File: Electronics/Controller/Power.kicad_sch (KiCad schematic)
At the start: 27 parts, among them J10 TABLET 1 PWR, J11 TABLET 2 PWR, J9 TRACTOR BATTERY, U5 LM2596S-5, U6 LM2587S-ADJ/NOPB, U7 LM2587S-ADJ/NOPB

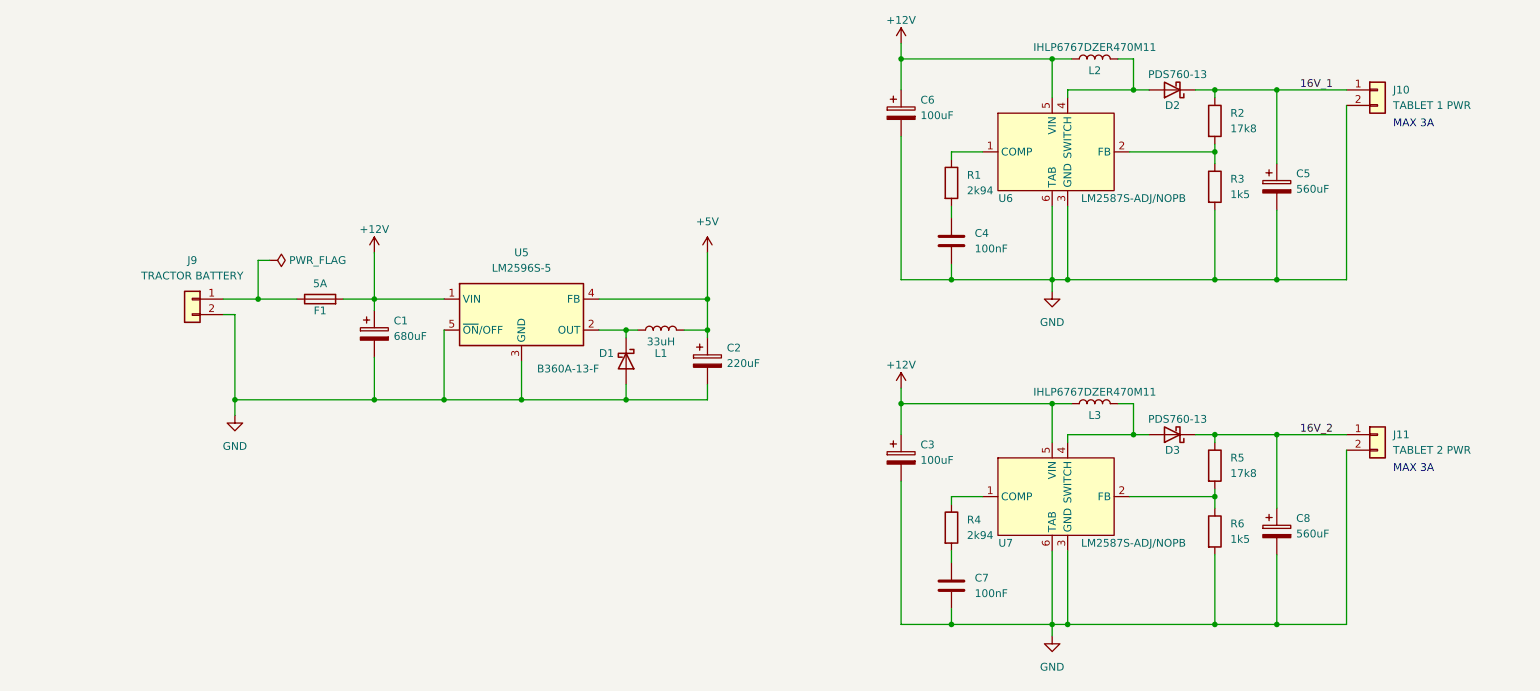
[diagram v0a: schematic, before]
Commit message: Working on schematic. Added datasheets.
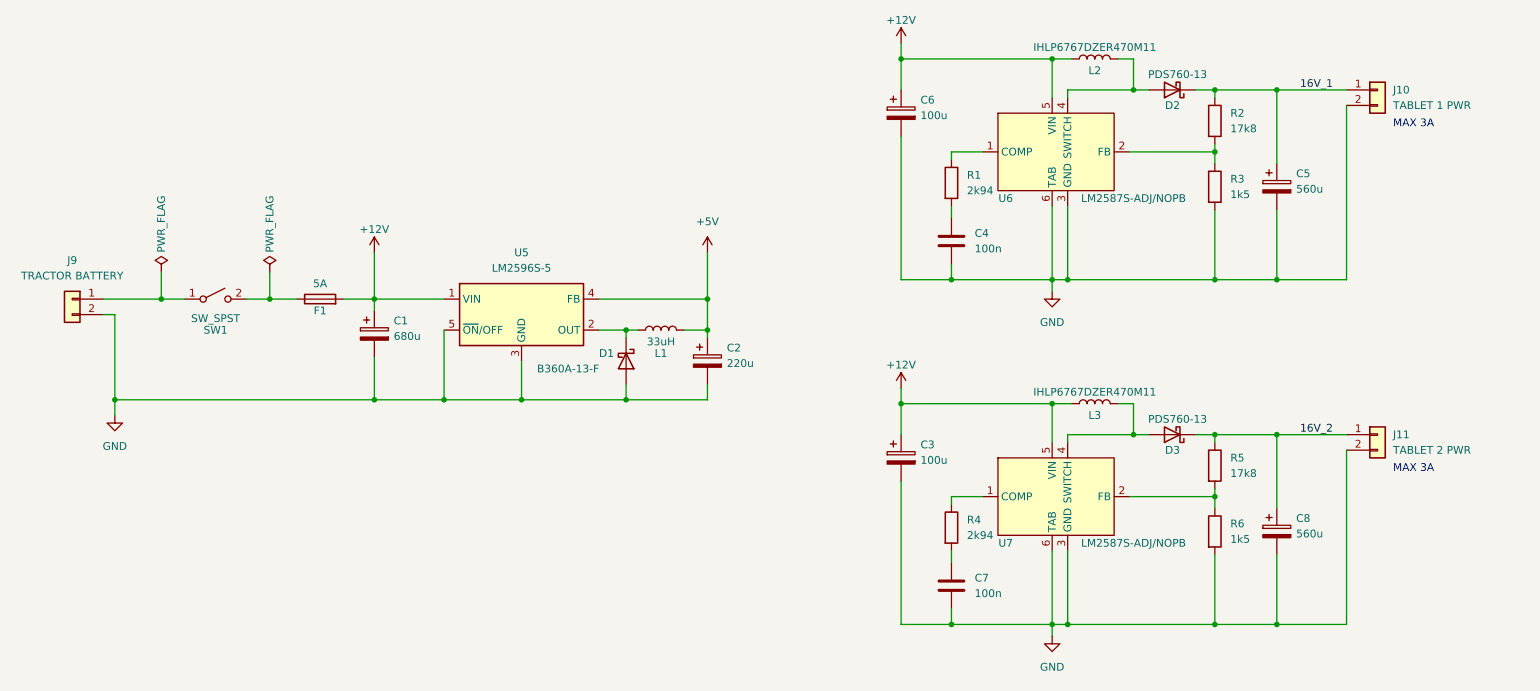
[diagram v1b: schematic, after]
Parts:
- added SW1: SW_SPST, symbol Switch:SW_SPST
- C1: value 680uF -> 680u
- C2: value 220uF -> 220u
- C3, C6: value 100uF -> 100u
- C4, C7: value 100nF -> 100n
- C5, C8: value 560uF -> 560u
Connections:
- net at J9.1 (Pin_1): now also SW1.1 (A); no longer F1.1
- new net: F1.1, SW1.2 (B)
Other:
- moved on the sheet: J9

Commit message: Working on schematic.
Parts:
- added J21: VALVE POWER, symbol Connector:Screw_Terminal_01x04
- F1: value 5A -> 10A
- SW1: value SW_SPST -> ON/OFF
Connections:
- net +12V: now also J21.1 (Pin_1), J21.3 (Pin_3)
- net GND: now also J21.2 (Pin_2), J21.4 (Pin_4)
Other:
- note added: "3A"
- note added: "3A per valve (=6A) 1.5A per tabler (=3A)"
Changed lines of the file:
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@@
   (title_block
     (title "Tandem Leveller Controller")
-    (date "2025-02-14")
+    (date "2025-02-16")
     (rev "V1.0")
     (company "(C) andy@britishideas.com 2025")
@@
   (junction (at 76.835 91.44) (diameter 0) (color 0 0 0 0)
   )
+  (junction (at 93.345 144.145) (diameter 0) (color 0 0 0 0)
+  )
   (junction (at 187.96 88.265) (diameter 0) (color 0 0 0 0)
   )
   (junction (at 171.45 144.78) (diameter 0) (color 0 0 0 0)
   )
+  (junction (at 91.44 136.525) (diameter 0) (color 0 0 0 0)
+  )
   (junction (at 163.195 108.585) (diameter 0) (color 0 0 0 0)
   )
@@
     (stroke (width 0) (type default))
   )
+  (wire (pts (xy 98.425 136.525) (xy 91.44 136.525))
+    (stroke (width 0) (type default))
+  )
   (wire (pts (xy 41.91 86.995) (xy 41.91 91.44))
     (stroke (width 0) (type default))
@@
     (stroke (width 0) (type default))
   )
+  (wire (pts (xy 93.345 139.065) (xy 93.345 144.145))
+    (stroke (width 0) (type default))
+  )
   (wire (pts (xy 131.445 91.44) (xy 131.445 96.52))
     (stroke (width 0) (type default))
@@
     (stroke (width 0) (type default))
   )
+  (wire (pts (xy 93.345 144.145) (xy 93.345 147.32))
+    (stroke (width 0) (type default))
+  )
   (wire (pts (xy 224.79 88.265) (xy 214.63 88.265))
     (stroke (width 0) (type default))
@@
     (stroke (width 0) (type default))
   )
+  (wire (pts (xy 91.44 141.605) (xy 91.44 136.525))
+    (stroke (width 0) (type default))
+  )
   (wire (pts (xy 163.195 106.045) (xy 163.195 108.585))
     (stroke (width 0) (type default))
@@
     (stroke (width 0) (type default))
   )
+  (wire (pts (xy 98.425 144.145) (xy 93.345 144.145))
+    (stroke (width 0) (type default))
+  )
   (wire (pts (xy 236.22 116.205) (xy 236.22 144.78))
     (stroke (width 0) (type default))
@@
     (stroke (width 0) (type default))
   )
+  (wire (pts (xy 98.425 141.605) (xy 91.44 141.605))
+    (stroke (width 0) (type default))
+  )
   (wire (pts (xy 100.965 107.95) (xy 88.265 107.95))
     (stroke (width 0) (type default))
@@
     (stroke (width 0) (type default))
   )
+  (wire (pts (xy 98.425 139.065) (xy 93.345 139.065))
+    (stroke (width 0) (type default))
+  )
   (wire (pts (xy 163.195 121.285) (xy 163.195 144.78))
     (stroke (width 0) (type default))
@@
   )
   (wire (pts (xy 236.22 59.69) (xy 236.22 88.265))
+    (stroke (width 0) (type default))
+  )
+  (wire (pts (xy 91.44 136.525) (xy 91.44 133.35))
     (stroke (width 0) (type default))
   )
@@
     (effects (font (size 1.27 1.27)) (justify left bottom))
   )
+  (text "3A per valve (=6A)\n1.5A per tabler (=3A)" (at 56.515 71.12 0)
+    (effects (font (size 1.27 1.27)) (justify left bottom))
+  )
+  (text "3A" (at 106.68 144.78 0)
+    (effects (font (size 1.27 1.27)) (justify left bottom))
+  )
   (label "16V_1" (at 228.6 57.15 0) (fields_autoplaced)
     (effects (font (size 1.27 1.27)) (justify left bottom))
@@
         (path "/56ffd1a6-bbed-43b6-8aa8-f23f49f76448/dcf28da0-a625-49c3-8f0d-066b6ff7258a"
           (reference "J10") (unit 1)
+        )
+      )
+    )
+  )
+  (symbol (lib_id "power:GND") (at 93.345 147.32 0) (unit 1)
+    (in_bom yes) (on_board yes) (dnp no) (fields_autoplaced)
+    (property "Reference" "#PWR087" (at 93.345 153.67 0)
+      (effects (font (size 1.27 1.27)) hide)
+    )
+    (property "Value" "GND" (at 93.345 152.4 0)
+      (effects (font (size 1.27 1.27)))
+    )
+    (property "Footprint" "" (at 93.345 147.32 0)
+      (effects (font (size 1.27 1.27)) hide)
+    )
+    (property "Datasheet" "" (at 93.345 147.32 0)
+      (effects (font (size 1.27 1.27)) hide)
+    )
+    (pin "1")
+    (instances
+      (project "Tandem Leveller Controller"
+        (path "/56ffd1a6-bbed-43b6-8aa8-f23f49f76448/dcf28da0-a625-49c3-8f0d-066b6ff7258a"
+          (reference "#PWR087") (unit 1)
+        )
+      )
+    )
+  )
+  (symbol (lib_id "power:+12V") (at 91.44 133.35 0) (unit 1)
+    (in_bom yes) (on_board yes) (dnp no)
+    (property "Reference" "#PWR088" (at 91.44 137.16 0)
+      (effects (font (size 1.27 1.27)) hide)
+    )
+    (property "Value" "+12V" (at 91.44 129.54 0)
+      (effects (font (size 1.27 1.27)))
+    )
+    (property "Footprint" "" (at 91.44 133.35 0)
+      (effects (font (size 1.27 1.27)) hide)
+    )
+    (property "Datasheet" "" (at 91.44 133.35 0)
+      (effects (font (size 1.27 1.27)) hide)
+    )
+    (pin "1")
+    (instances
+      (project "Tandem Leveller Controller"
+        (path "/56ffd1a6-bbed-43b6-8aa8-f23f49f76448/dcf28da0-a625-49c3-8f0d-066b6ff7258a"
+          (reference "#PWR088") (unit 1)
         )
       )
@@
     )
   )
+  (symbol (lib_id "Connector:Screw_Terminal_01x04") (at 103.505 139.065 0) (unit 1)
+    (in_bom yes) (on_board yes) (dnp no) (fields_autoplaced)
+    (property "Reference" "J21" (at 106.68 139.065 0)
+      (effects (font (size 1.27 1.27)) (justify left))
+    )
+    (property "Value" "VALVE POWER" (at 106.68 141.605 0)
+      (effects (font (size 1.27 1.27)) (justify left))
+    )
+    (property "Footprint" "" (at 103.505 139.065 0)
+      (effects (font (size 1.27 1.27)) hide)
+    )
+    (property "Datasheet" "~" (at 103.505 139.065 0)
+      (effects (font (size 1.27 1.27)) hide)
+    )
+    (pin "3")
+    (pin "4")
+    (pin "1")
+    (pin "2")
+    (instances
+      (project "Tandem Leveller Controller"
+        (path "/56ffd1a6-bbed-43b6-8aa8-f23f49f76448/dcf28da0-a625-49c3-8f0d-066b6ff7258a"
+          (reference "J21") (unit 1)
+        )
+      )
+    )
+  )
   (symbol (lib_id "Device:C_Polarized") (at 163.195 60.96 0) (unit 1)
     (in_bom yes) (on_board yes) (dnp no)
@@
   (symbol (lib_id "Switch:SW_SPST") (at 50.8 91.44 0) (unit 1)
     (in_bom yes) (on_board yes) (dnp no)
-    (property "Reference" "SW1" (at 50.8 96.52 0)
-      (effects (font (size 1.27 1.27)))
-    )
-    (property "Value" "SW_SPST" (at 50.8 94.615 0)
+    (property "Reference" "SW1" (at 50.8 88.265 0)
+      (effects (font (size 1.27 1.27)))
+    )
+    (property "Value" "ON/OFF" (at 50.8 94.615 0)
       (effects (font (size 1.27 1.27)))
     )
@@
       (effects (font (size 1.27 1.27)))
     )
-    (property "Value" "5A" (at 67.945 88.9 90)
-      (effects (font (size 1.27 1.27)))
-    )
+    (property "Value" "10A" (at 67.945 88.9 90)
+      (effects (font (size 1.27 1.27)))
+    )

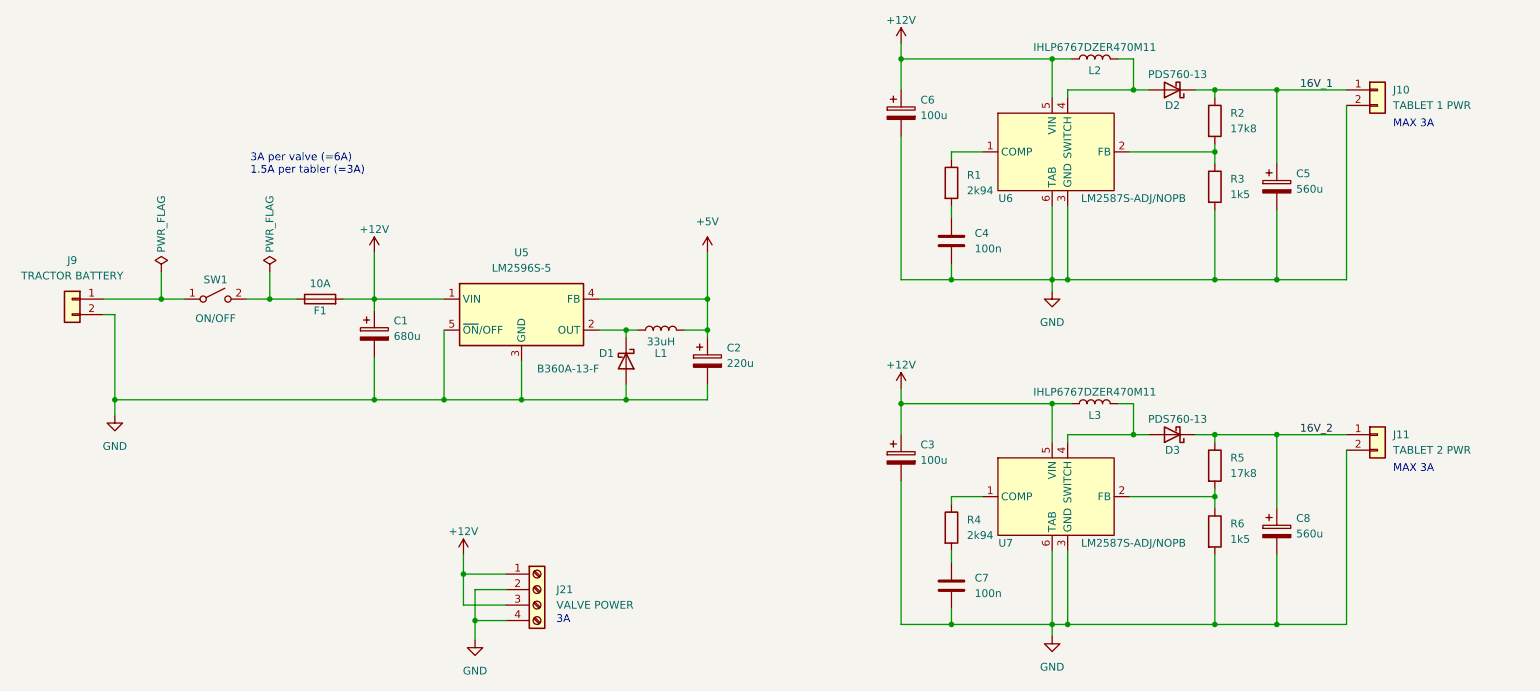
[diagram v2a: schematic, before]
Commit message: Updated schematic. Added footprints for all components.
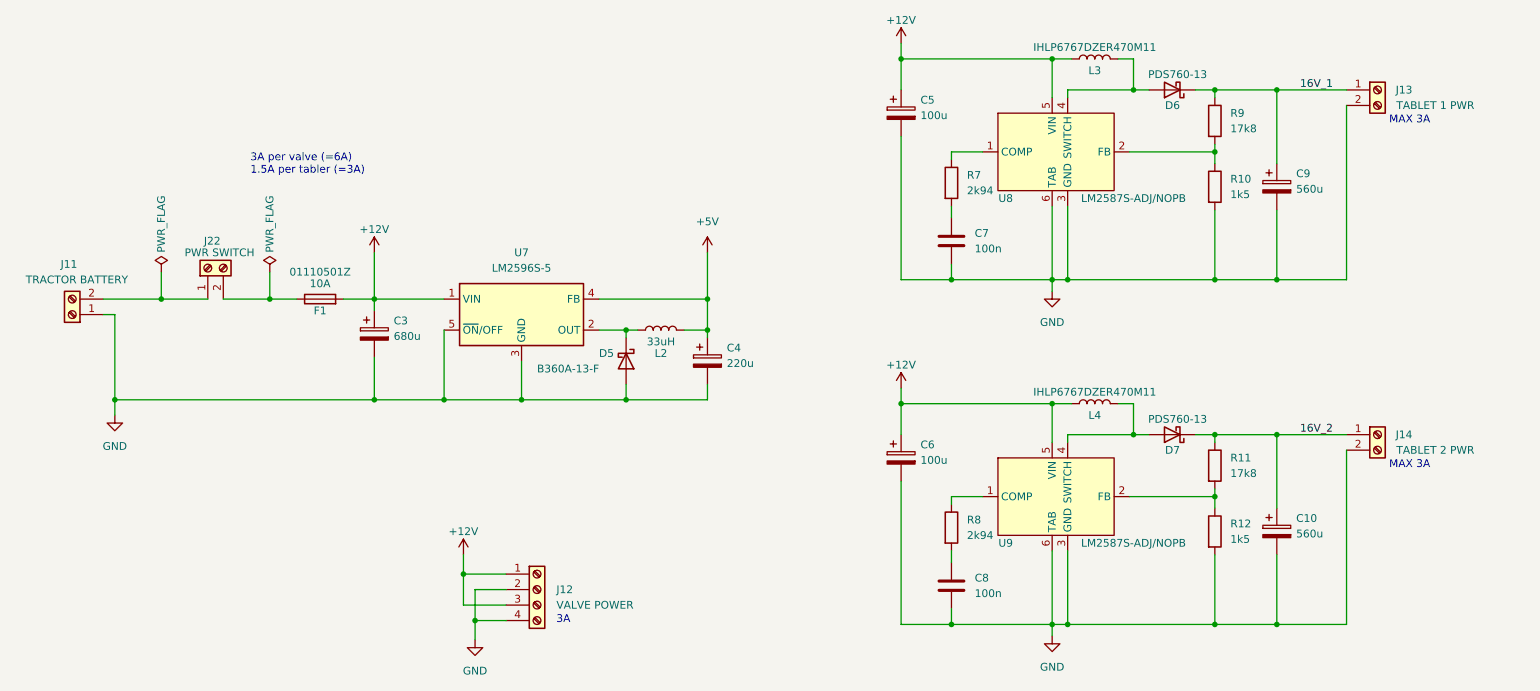
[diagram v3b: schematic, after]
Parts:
- removed J10: TABLET 1 PWR, symbol Connector_Generic:Conn_01x02
- removed J11: TABLET 2 PWR, symbol Connector_Generic:Conn_01x02
- removed J9: TRACTOR BATTERY, symbol Connector_Generic:Conn_01x02
- removed SW1: ON/OFF, symbol Switch:SW_SPST
- added J11: TRACTOR BATTERY, Britishideas:PhoenixContact_COMBICON_MKDSN_2, symbol Connector:Screw_Terminal_01x02
- added J13: TABLET 1 PWR, Britishideas:PhoenixContact_COMBICON_MKDSN_2, symbol Connector:Screw_Terminal_01x02
- added J14: TABLET 2 PWR, Britishideas:PhoenixContact_COMBICON_MKDSN_2, symbol Connector:Screw_Terminal_01x02
- added J22: PWR SWITCH, Britishideas:PhoenixContact_COMBICON_MKDSN_2, symbol Connector:Screw_Terminal_01x02
- C10: renamed from C8; footprint (none) -> Capacitor_SMD:CP_Elec_10x10.5; manf# (none) -> EMZR350ARA561MJA0G
- C3: renamed from C1; footprint (none) -> Capacitor_SMD:CP_Elec_10x10.5
- C4: renamed from C2; footprint (none) -> Capacitor_SMD:CP_Elec_8x6.5
- C5: renamed from C6; footprint (none) -> Capacitor_SMD:CP_Elec_6.3x5.9; manf# (none) -> UUD1C101MCL1GS
- C6: renamed from C3; footprint (none) -> Capacitor_SMD:CP_Elec_6.3x5.9; manf# (none) -> UUD1C101MCL1GS
- C7: renamed from C4; footprint (none) -> Capacitor_SMD:C_0805_2012Metric
- C8: renamed from C7; footprint (none) -> Capacitor_SMD:C_0805_2012Metric
- C9: renamed from C5; footprint (none) -> Capacitor_SMD:CP_Elec_10x10.5; manf# (none) -> EMZR350ARA561MJA0G
- D5: renamed from D1; footprint (none) -> Diode_SMD:D_SMA
- D6: renamed from D2; footprint (none) -> Diode_SMD:D_PowerDI-5
- D7: renamed from D3; footprint (none) -> Diode_SMD:D_PowerDI-5
- F1: footprint (none) -> Britishideas:5x20 Fuse Holder; manf# (none) -> 01110501Z
- J12: renamed from J21; footprint (none) -> Britishideas:PhoenixContact_COMBICON_PT_4; manf# (none) -> 1729034
- L2: renamed from L1; footprint (none) -> Britishideas:Chilisin_Power_Inductor_AWVS_808040
- L3: renamed from L2; footprint (none) -> Britishideas:IHLP6767DZER470M11
- L4: renamed from L3; footprint (none) -> Britishideas:IHLP6767DZER470M11
- R10: renamed from R3; footprint (none) -> Resistor_SMD:R_0805_2012Metric
- R11: renamed from R5; footprint (none) -> Resistor_SMD:R_0805_2012Metric
- R12: renamed from R6; footprint (none) -> Resistor_SMD:R_0805_2012Metric
- R7: renamed from R1; footprint (none) -> Resistor_SMD:R_0805_2012Metric
- R8: renamed from R4; footprint (none) -> Resistor_SMD:R_0805_2012Metric
- R9: renamed from R2; footprint (none) -> Resistor_SMD:R_0805_2012Metric
- renumbered U5 to U7, U6 to U8, U7 to U9
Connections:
- net 16V_1: now also J13.1 (Pin_1)
- net 16V_2: now also J14.1 (Pin_1)
- net GND: now also J11.1 (Pin_1), J13.2 (Pin_2), J14.2 (Pin_2)
- net at F1.1: now also J22.2 (Pin_2)
- new net: J11.2 (Pin_2), J22.1 (Pin_1)

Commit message: Changed switches and lamps. Removed status LEDs. Working on PCB layout.
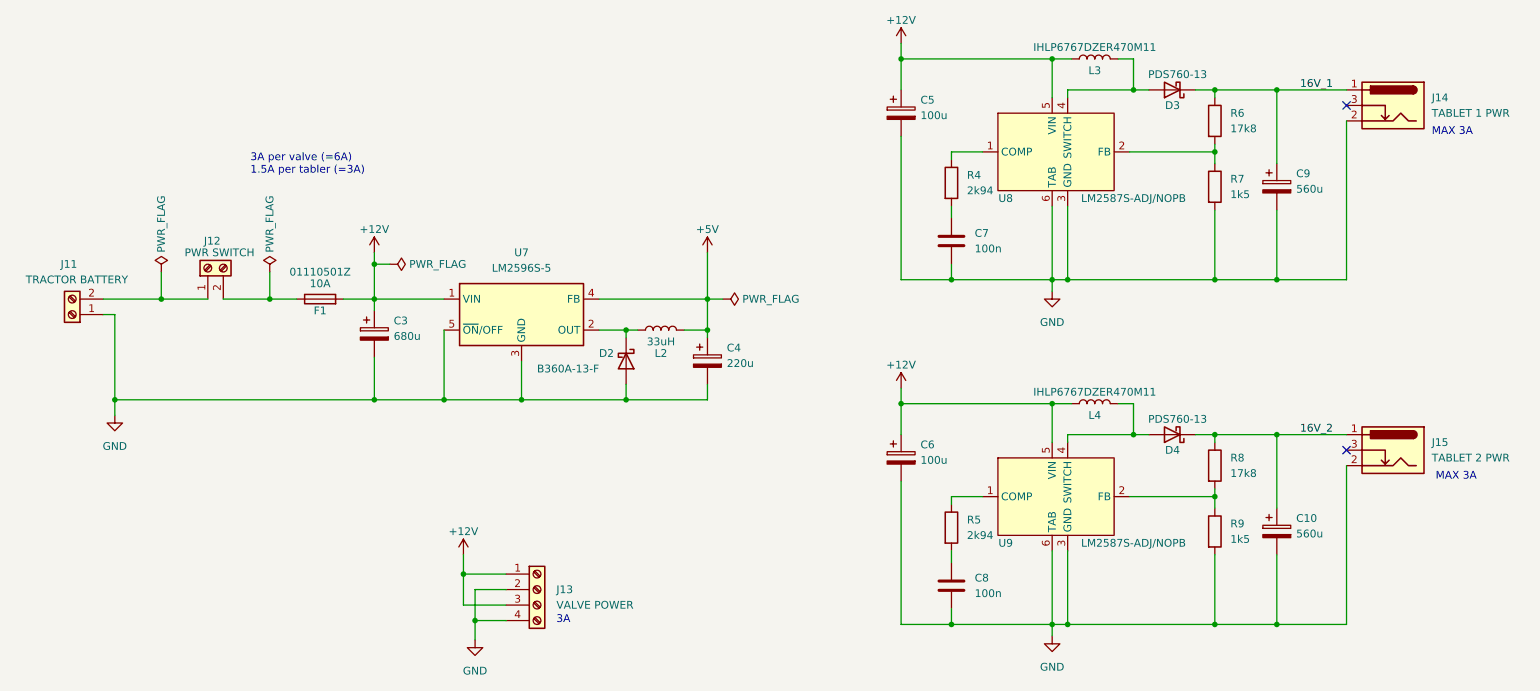
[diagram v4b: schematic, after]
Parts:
- removed J13: TABLET 1 PWR, Britishideas:PhoenixContact_COMBICON_MKDSN_2, symbol Connector:Screw_Terminal_01x02
- removed J14: TABLET 2 PWR, Britishideas:PhoenixContact_COMBICON_MKDSN_2, symbol Connector:Screw_Terminal_01x02
- added J14: TABLET 1 PWR, Connector_BarrelJack:BarrelJack_Wuerth_6941xx301002, symbol Connector:Barrel_Jack_Switch
- added J15: TABLET 2 PWR, Connector_BarrelJack:BarrelJack_Wuerth_6941xx301002, symbol Connector:Barrel_Jack_Switch
- renumbered D5 to D2, D6 to D3, D7 to D4, J22 to J12, J12 to J13, R7 to R4, R8 to R5, R9 to R6, R10 to R7, R11 to R8, R12 to R9
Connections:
- net 16V_1: now also J14.1
- net 16V_2: now also J15.1
- net GND: now also J14.2, J15.2
- no-connect marks 0 -> 2
